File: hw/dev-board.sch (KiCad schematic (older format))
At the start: 65 parts, among them CON1 BARREL_JACK, IC1 FDG6331L, P1 USB_OTG, P10 CONN_01X06, P11 CONN_01X08, P2 CONN_02X03_ICSP, P3 CONN_02X03, P4 CONN_02X03_ICSP, P5 CONN_01X08, P6 CONN_02X03, P7 CONN_02X03_ICSP, P8 CONN_02X03_ICSP, P9 CONN_01X10, Q1 FDN340P, SW1 SW_PUSH, U1 LM2940LD-5.0, U10 TS3A44159, U2 MIC5205, U3 ATMEGA16U2, U4 23K256, U5 ATTINY85-SUR, U6 TS3A44159, U7 ATMEGA328PB-MU, U8 74LVCH1T45, U9 ATTINY85-SUR, X1 CRYSTAL, X2 RESONATOR

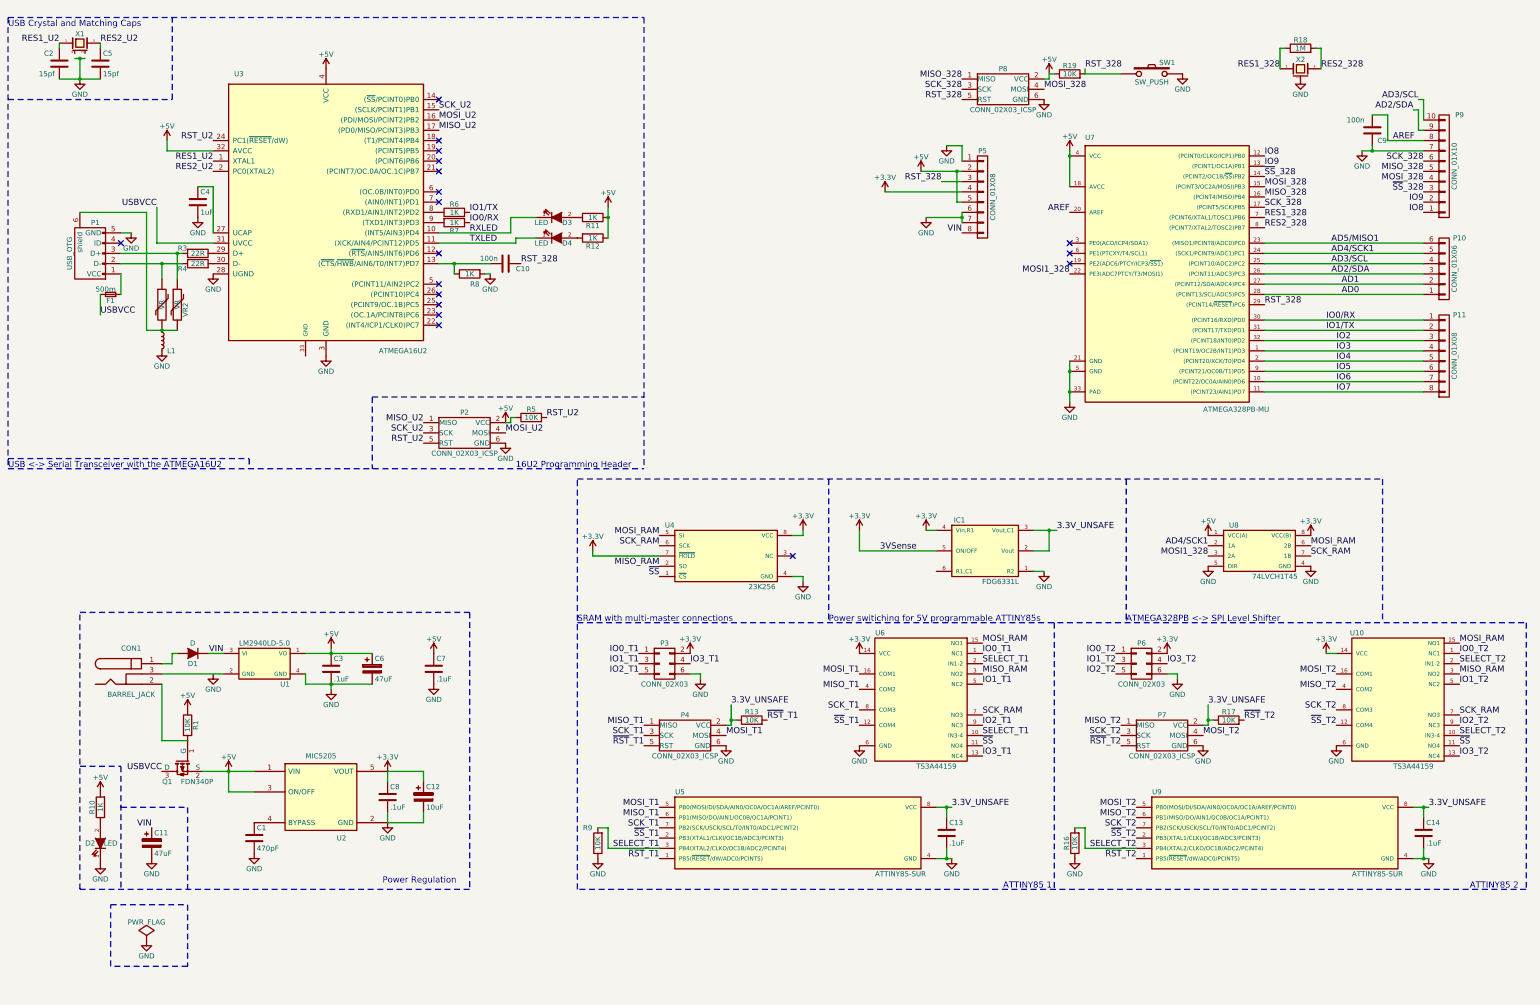
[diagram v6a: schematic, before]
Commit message: Coarse placement of power and usb passives. All components are on board. Connectors have the correct footprint. Tinys need better placement. Final adjustments will make placing traces easier.
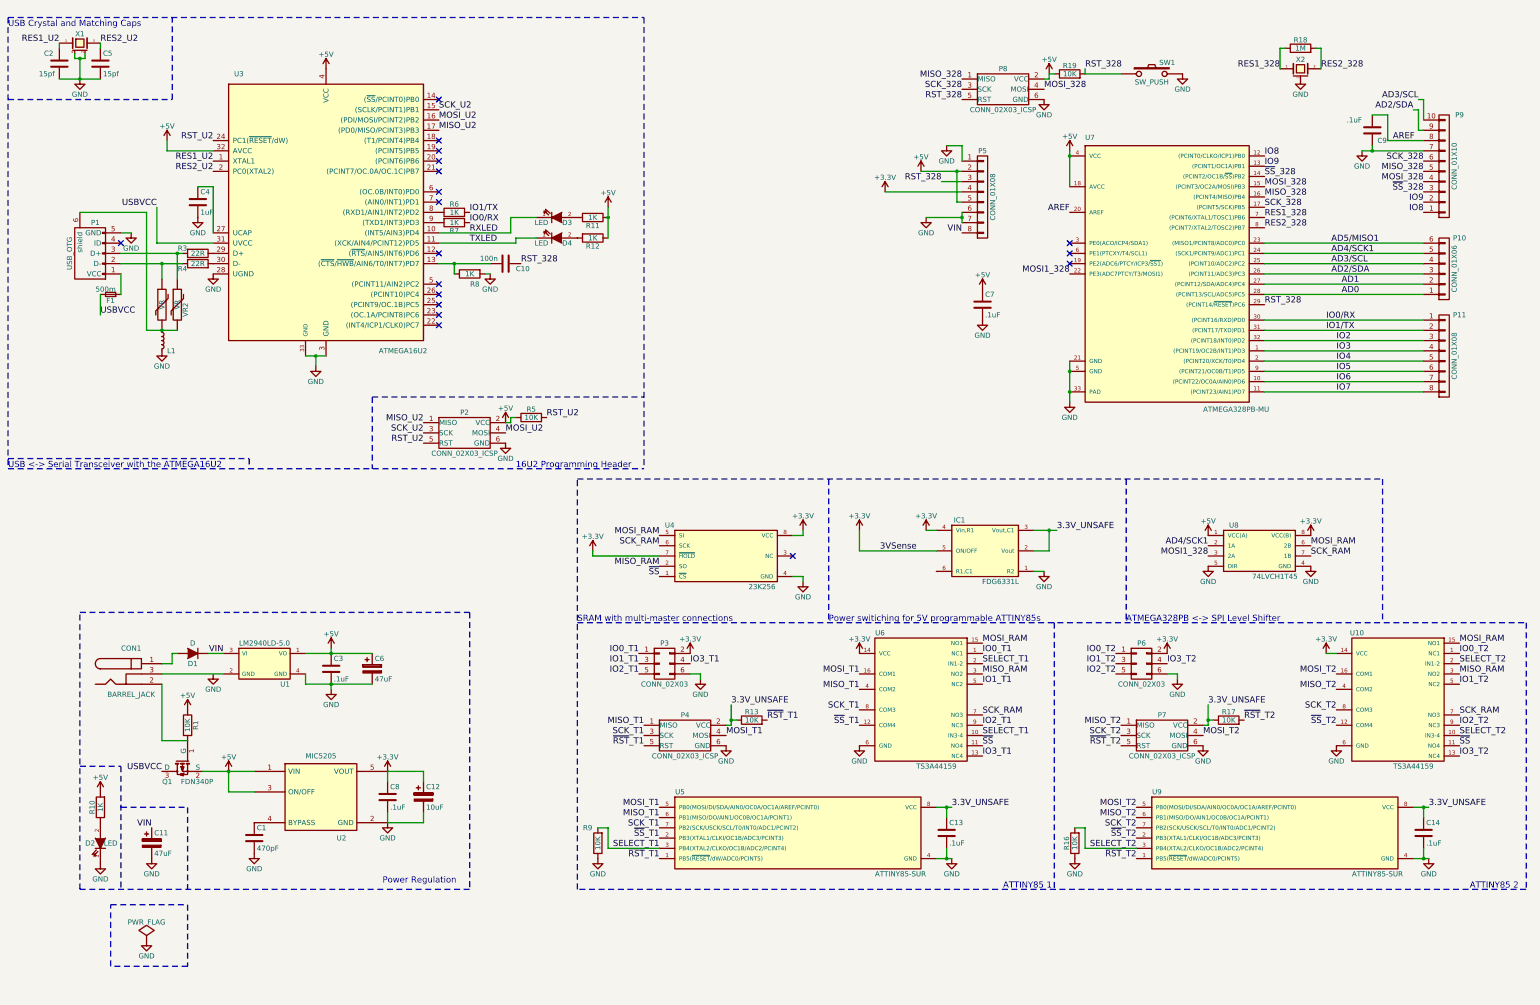
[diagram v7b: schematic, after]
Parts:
- C9: value 100n -> .1uF
- U8: footprint TO_SOT_Packages_SMD:SOT-886 -> Housings_SSOP:MSOP-8_3x3mm_Pitch0.65mm
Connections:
- net GND: now also U3.33 (GND), X1.2 (case), X1.4 (0.508)
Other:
- moved on the sheet: C7
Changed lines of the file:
@@
 L GND #PWR02
 U 1 1 5756DC7D
-P 4000 4300
-F 0 "#PWR02" H 4000 4050 50  0001 C CNN
-F 1 "GND" H 4000 4150 50  0000 C CNN
-F 2 "" H 4000 4300 50  0000 C CNN
-F 3 "" H 4000 4300 50  0000 C CNN
-	1    4000 4300
+P 3900 4400
+F 0 "#PWR02" H 3900 4150 50  0001 C CNN
+F 1 "GND" H 3900 4250 50  0000 C CNN
+F 2 "" H 3900 4400 50  0000 C CNN
+F 3 "" H 3900 4400 50  0000 C CNN
+	1    3900 4400
 	1    0    0    -1
 $EndComp
@@
 P 14200 2100
 F 0 "C9" H 14250 2000 50  0000 L CNN
-F 1 "100n" H 13950 2200 50  0000 L CNN
+F 1 ".1uF" H 13950 2200 50  0000 L CNN
 F 2 "Capacitors_SMD:C_0603" H 14238 1950 50  0001 C CNN
 F 3 "" H 14200 2100 50  0000 C CNN
@@
 L +5V #PWR016
 U 1 1 575A8256
-P 5050 7200
-F 0 "#PWR016" H 5050 7050 50  0001 C CNN
-F 1 "+5V" H 5050 7340 50  0000 C CNN
-F 2 "" H 5050 7200 50  0000 C CNN
-F 3 "" H 5050 7200 50  0000 C CNN
-	1    5050 7200
+P 10400 3650
+F 0 "#PWR016" H 10400 3500 50  0001 C CNN
+F 1 "+5V" H 10400 3790 50  0000 C CNN
+F 2 "" H 10400 3650 50  0000 C CNN
+F 3 "" H 10400 3650 50  0000 C CNN
+	1    10400 3650
 	1    0    0    -1
 $EndComp
@@
 L GND #PWR017
 U 1 1 575A82B2
-P 5050 7500
-F 0 "#PWR017" H 5050 7250 50  0001 C CNN
-F 1 "GND" H 5050 7350 50  0000 C CNN
-F 2 "" H 5050 7500 50  0000 C CNN
-F 3 "" H 5050 7500 50  0000 C CNN
-	1    5050 7500
+P 10400 3950
+F 0 "#PWR017" H 10400 3700 50  0001 C CNN
+F 1 "GND" H 10400 3800 50  0000 C CNN
+F 2 "" H 10400 3950 50  0000 C CNN
+F 3 "" H 10400 3950 50  0000 C CNN
+	1    10400 3950
 	1    0    0    -1
 $EndComp
@@
 L C C7
 U 1 1 575A830E
-P 5050 7350
-F 0 "C7" H 5075 7450 50  0000 L CNN
-F 1 ".1uF" H 5075 7250 50  0000 L CNN
-F 2 "Capacitors_SMD:C_0603" H 5088 7200 50  0001 C CNN
-F 3 "" H 5050 7350 50  0000 C CNN
-	1    5050 7350
+P 10400 3800
+F 0 "C7" H 10425 3900 50  0000 L CNN
+F 1 ".1uF" H 10425 3700 50  0000 L CNN
+F 2 "Capacitors_SMD:C_0603" H 10438 3650 50  0001 C CNN
+F 3 "" H 10400 3800 50  0000 C CNN
+	1    10400 3800
 	1    0    0    -1
 $EndComp
@@
 F 0 "U8" H 12850 6450 50  0000 C CNN
 F 1 "74LVCH1T45" H 13250 5950 50  0000 C CNN
-F 2 "TO_SOT_Packages_SMD:SOT-886" H 13100 5850 50  0001 C CIN
+F 2 "Housings_SSOP:MSOP-8_3x3mm_Pitch0.65mm" H 13100 5850 50  0001 C CIN
 F 3 "" H 13100 6200 50  0000 C CNN
 	1    13100 6200
@@
 Wire Notes Line
 	3250 5300 3250 5400
+Wire Wire Line
+	1550 1350 1550 1400
+Wire Wire Line
+	1650 1400 1650 1350
+Wire Wire Line
+	3800 4300 4000 4300
+Wire Wire Line
+	3900 4300 3900 4400
+Connection ~ 3900 4300
 $EndSCHEMATC

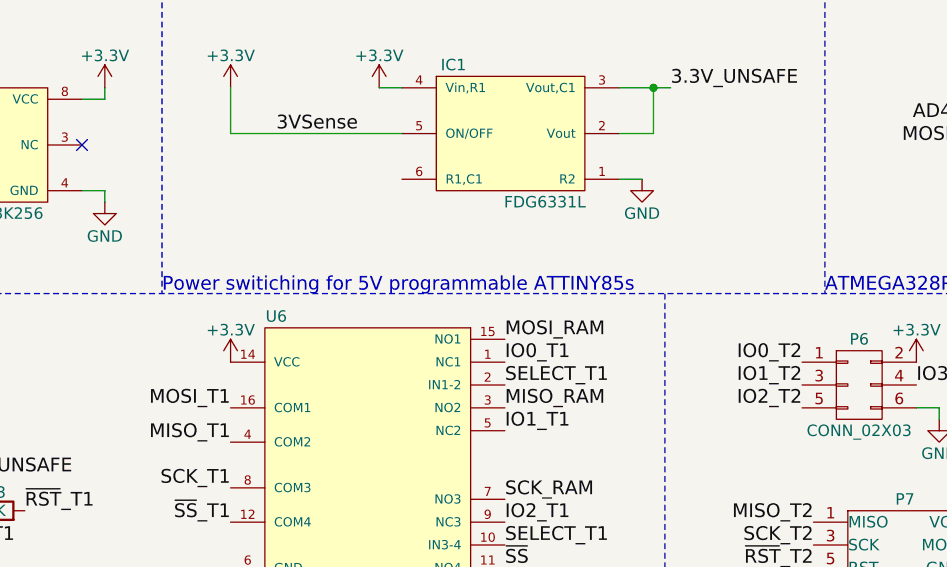
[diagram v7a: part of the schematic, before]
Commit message: Semi-Final PCB layout. Missing R1 for load switch. Pre-traces
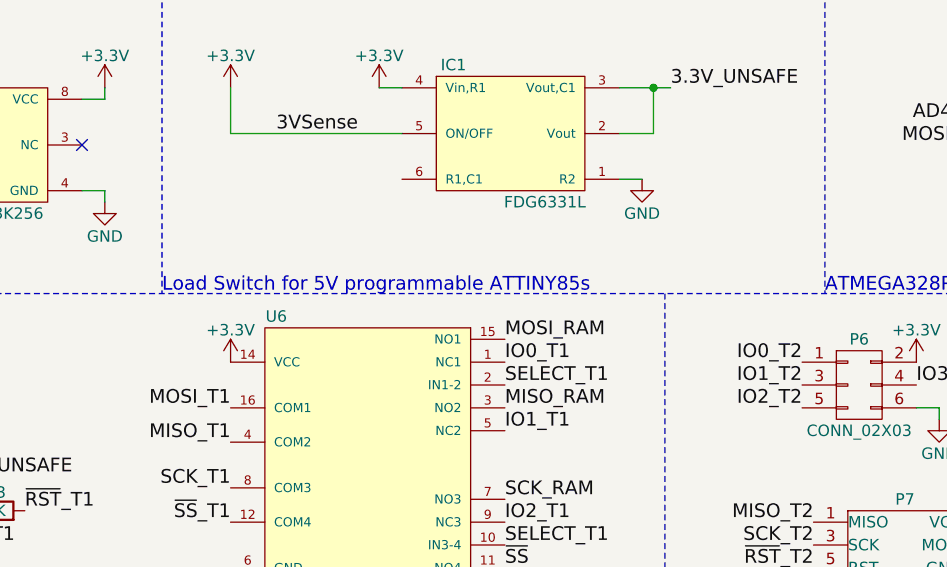
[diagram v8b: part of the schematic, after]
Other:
- note added: "Load Switch for 5V programmable ATTINY85s"
- note removed: "Power switiching for 5V programmable ATTINY85s"
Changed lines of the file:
@@
 	14700 3600 13150 3600
 Text Notes 8900 6900 0    60   ~ 0
-Power switiching for 5V programmable ATTINY85s
+Load Switch for 5V programmable ATTINY85s
 Text Notes 6450 6900 0    60   ~ 0
 SRAM with multi-master connections
